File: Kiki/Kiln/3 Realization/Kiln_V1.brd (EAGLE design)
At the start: 100 x 80 mm, 19 parts, among them T1 2N3904, T2 2N3904, T3 2N3904, T4 2N3904

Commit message: Updated: 3.3v & GND Disconnected the 3.3v pin -- the was a supply pin, not a power in pin. Attached the GND for the transistors to BOTH Arduino ground pins, and beefec up the trace, just in case.  I wonder if this is enough to dump the transistors, when all segments of the digit are illuminated?
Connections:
- removed net N$30: JP3.8, PCB1.3.3V
- net GND: now also PCB1.GND., PCB1.GND..
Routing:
- net N$30: track 69.9 -> 0.00 mm
- net GND: track 35.6 -> 66.0 mm
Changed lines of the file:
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@@
 <wire x1="68.58" y1="59.69" x2="68.58" y2="50.38" width="0.4064" layer="1"/>
-</signal>
-<signal name="N$30">
-<contactref element="JP3" pad="8"/>
-<contactref element="PCB1" pad="3.3V"/>
-<wire x1="41.91" y1="49.53" x2="41.91" y2="53.34" width="0.4064" layer="1"/>
-<wire x1="41.91" y1="53.34" x2="36.83" y2="53.34" width="0.4064" layer="1"/>
-<wire x1="36.83" y1="53.34" x2="36.83" y2="15.24" width="0.4064" layer="1"/>
-<wire x1="36.83" y1="15.24" x2="55.88" y2="15.24" width="0.4064" layer="1"/>
-<wire x1="55.88" y1="15.24" x2="55.88" y2="11.43" width="0.4064" layer="1"/>
 </signal>
 <signal name="N$31">
 <contactref element="JP3" pad="9"/>
 <contactref element="PCB1" pad="VIN"/>
-<wire x1="39.37" y1="49.53" x2="39.37" y2="17.78" width="0.4064" layer="1"/>
-<wire x1="39.37" y1="17.78" x2="58.42" y2="17.78" width="0.4064" layer="1"/>
-<wire x1="58.42" y1="17.78" x2="58.42" y2="13.97" width="0.4064" layer="1"/>
-<wire x1="58.42" y1="13.97" x2="66.04" y2="13.97" width="0.4064" layer="1"/>
-<wire x1="66.04" y1="13.97" x2="66.04" y2="11.43" width="0.4064" layer="1"/>
+<wire x1="66.04" y1="11.43" x2="66.04" y2="17.78" width="0.4064" layer="16"/>
+<wire x1="66.04" y1="17.78" x2="58.42" y2="17.78" width="0.4064" layer="16"/>
+<wire x1="58.42" y1="17.78" x2="58.42" y2="24.13" width="0.4064" layer="16"/>
+<wire x1="58.42" y1="24.13" x2="39.37" y2="24.13" width="0.4064" layer="16"/>
+<wire x1="39.37" y1="24.13" x2="39.37" y2="49.53" width="0.4064" layer="16"/>
 </signal>
 <signal name="N$28">
@@
 <contactref element="T2" pad="3"/>
 <contactref element="T1" pad="3"/>
+<contactref element="PCB1" pad="GND."/>
+<contactref element="PCB1" pad="GND.."/>
+<wire x1="60.96" y1="16.51" x2="60.96" y2="11.43" width="0.4064" layer="1"/>
+<wire x1="63.5" y1="11.43" x2="63.5" y2="16.51" width="0.4064" layer="1"/>
+<wire x1="86.36" y1="26.67" x2="78.74" y2="26.67" width="0.8128" layer="1"/>
+<wire x1="78.74" y1="26.67" x2="71.12" y2="26.67" width="0.8128" layer="1"/>
+<wire x1="71.12" y1="26.67" x2="63.5" y2="26.67" width="0.8128" layer="1"/>
+<wire x1="63.5" y1="26.67" x2="58.42" y2="26.67" width="0.8128" layer="1"/>
+<wire x1="58.42" y1="26.67" x2="58.42" y2="16.51" width="0.8128" layer="1"/>
+<wire x1="58.42" y1="16.51" x2="60.96" y2="16.51" width="0.8128" layer="1"/>
+<wire x1="60.96" y1="16.51" x2="63.5" y2="16.51" width="0.8128" layer="1"/>
+<wire x1="86.36" y1="22.86" x2="86.36" y2="26.67" width="0.4064" layer="1"/>
+<wire x1="78.74" y1="24.13" x2="78.74" y2="26.67" width="0.4064" layer="1"/>
+<wire x1="71.12" y1="24.13" x2="71.12" y2="26.67" width="0.4064" layer="1"/>
 <wire x1="63.5" y1="22.86" x2="63.5" y2="26.67" width="0.4064" layer="1"/>
-<wire x1="63.5" y1="26.67" x2="71.12" y2="26.67" width="0.4064" layer="1"/>
-<wire x1="71.12" y1="24.13" x2="71.12" y2="26.67" width="0.4064" layer="1"/>
-<wire x1="71.12" y1="26.67" x2="78.74" y2="26.67" width="0.4064" layer="1"/>
-<wire x1="78.74" y1="24.13" x2="78.74" y2="26.67" width="0.4064" layer="1"/>
-<wire x1="78.74" y1="26.67" x2="86.36" y2="26.67" width="0.4064" layer="1"/>
-<wire x1="86.36" y1="26.67" x2="86.36" y2="22.86" width="0.4064" layer="1"/>
 </signal>
 <signal name="N$9">

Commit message: Update: minor changes Changed the name of the Thermal Amplifier JP3 connector, for clarity.
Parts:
- renumbered JP3 to JP3-THERM-AMP
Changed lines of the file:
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@@
 <element name="T3" library="transistor" package="TO92" value="2N3904" x="77.47" y="24.13" rot="R180"/>
 <element name="T4" library="transistor" package="TO92" value="2N3904" x="85.09" y="22.86" rot="R180"/>
-<element name="JP3" library="microbuilder" package="1X09_ROUND_70" value="" x="49.53" y="49.53" rot="R180"/>
+<element name="JP3-THERM-AMP" library="microbuilder" package="1X09_ROUND_70" value="" x="49.53" y="49.53" rot="R180"/>
 </elements>
 <signals>
@@
 </signal>
 <signal name="DRDY">
-<contactref element="JP3" pad="1"/>
+<contactref element="JP3-THERM-AMP" pad="1"/>
 </signal>
 <signal name="SCK">
-<contactref element="JP3" pad="6"/>
+<contactref element="JP3-THERM-AMP" pad="6"/>
 <contactref element="PCB1" pad="13"/>
 <wire x1="49.276" y1="59.69" x2="49.53" y2="59.69" width="0.4064" layer="1"/>
@@
 </signal>
 <signal name="SDO">
-<contactref element="JP3" pad="5"/>
+<contactref element="JP3-THERM-AMP" pad="5"/>
 <contactref element="PCB1" pad="12"/>
 <wire x1="51.816" y1="59.69" x2="52.07" y2="59.69" width="0.4064" layer="1"/>
@@
 </signal>
 <signal name="SDI">
-<contactref element="JP3" pad="4"/>
+<contactref element="JP3-THERM-AMP" pad="4"/>
 <contactref element="PCB1" pad="11"/>
 <wire x1="54.356" y1="59.69" x2="54.61" y2="59.69" width="0.4064" layer="1"/>
@@
 </signal>
 <signal name="!CS">
-<contactref element="JP3" pad="3"/>
+<contactref element="JP3-THERM-AMP" pad="3"/>
 <contactref element="PCB1" pad="10"/>
 <wire x1="56.896" y1="59.69" x2="57.15" y2="59.69" width="0.4064" layer="1"/>
@@
 </signal>
 <signal name="!FAULT">
-<contactref element="JP3" pad="2"/>
+<contactref element="JP3-THERM-AMP" pad="2"/>
 </signal>
 <signal name="N$22">
@@
 </signal>
 <signal name="N$31">
-<contactref element="JP3" pad="9"/>
+<contactref element="JP3-THERM-AMP" pad="9"/>
 <contactref element="PCB1" pad="VIN"/>
 <wire x1="66.04" y1="11.43" x2="66.04" y2="17.78" width="0.4064" layer="16"/>
@@
 <signal name="N$28">
 <contactref element="PCB1" pad="GND"/>
-<contactref element="JP3" pad="7"/>
+<contactref element="JP3-THERM-AMP" pad="7"/>
 <wire x1="46.736" y1="59.69" x2="46.99" y2="59.69" width="0.4064" layer="1"/>
 <wire x1="46.99" y1="59.69" x2="46.99" y2="57.15" width="0.4064" layer="1"/>

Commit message: Update: new display The display file was the wrong size.  Rebuilt it. Layout got horked, so had to rebuild it from scratch. Also added the relay and Heating indicator light.
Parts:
- removed 4DIG_7SEG1: (no value), 7-seg-disp:4DIG_7SEG
- added LED1: (no value), 1-Generic:LED3MM
- added R-REPLACE_ME: 0.1OHM-1/2W-1%(1210), SparkFun-Resistors:1210
- added U$1: 4DIG_7SEG_056, 7-seg-disp:4DIG_7SEG_056
- added X1: 3.5mm term, microbuilder:TERMBLOCK_1X2-3.5MM
- R10, R11, R8, R9: value (none) -> 4.7K
- moved JP3-THERM-AMP 16.3 mm to (39.4, 36.8), turned to 270 degrees
- moved R1 5.08 mm to (63.5, 54.6)
- moved R2 5.08 mm to (66.0, 54.6)
- moved R3 5.08 mm to (68.6, 54.6)
- moved R4 5.08 mm to (71.1, 54.6)
- moved R5 5.08 mm to (73.7, 54.6)
- moved R6 5.08 mm to (76.2, 54.6)
- moved R7 5.08 mm to (78.7, 54.6)
- moved R10 4.58 mm to (76.2, 15.2)
- moved R11 4.58 mm to (78.7, 15.2)
- moved R8 4.58 mm to (71.1, 15.2)
- moved R9 4.58 mm to (73.7, 15.2)
- moved FRAME1 1.27 mm to (17.8, 81.3)
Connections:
- removed net !FAULT: JP3-THERM-AMP.2
- removed net DRDY: JP3-THERM-AMP.1
- removed net N$28: JP3-THERM-AMP.7, PCB1.GND
- new net N$21: LED1.A, R-REPLACE_ME.2
- new net RELAY_POS: PCB1.9, R-REPLACE_ME.1, X1.1
- net GND: now also JP3-THERM-AMP.7, LED1.K, PCB1.GND, X1.2
- net N$10: now also U$1.13; no longer 4DIG_7SEG1.13
- net N$11: now also U$1.9; no longer 4DIG_7SEG1.9
- net N$12: now also U$1.4; no longer 4DIG_7SEG1.4
- net N$13: now also U$1.2; no longer 4DIG_7SEG1.2
- net N$14: now also U$1.1; no longer 4DIG_7SEG1.1
- net N$15: now also U$1.12; no longer 4DIG_7SEG1.12
- net N$16: now also U$1.5; no longer 4DIG_7SEG1.5
- net N$17: now also PCB1.A3; no longer PCB1.A5
- net N$18: now also PCB1.A2; no longer PCB1.A4
- net N$19: now also PCB1.A1; no longer PCB1.A3
- net N$20: now also PCB1.A0; no longer PCB1.A2
- net N$5: now also U$1.6; no longer 4DIG_7SEG1.6
- net N$6: now also U$1.10; no longer 4DIG_7SEG1.10
- net N$7: now also U$1.11; no longer 4DIG_7SEG1.11
- net N$8: now also U$1.14; no longer 4DIG_7SEG1.14
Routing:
- net GND: track 66.0 -> 156.9 mm, vias 0 -> 1
- net RELAY_POS: track 0.00 -> 53.1 mm, vias 0 -> 2
- net SDO: track 13.0 -> 35.8 mm, vias 0 -> 1
- net SCK: track 13.0 -> 35.8 mm
- net !CS: track 13.0 -> 35.8 mm, vias 0 -> 1
- net N$31: track 64.8 -> 41.9 mm
- net SDI: track 13.0 -> 35.3 mm, vias 0 -> 1
- net N$12: track 60.1 -> 39.8 mm, vias 1 -> 2
- net N$15: track 34.7 -> 16.9 mm, vias 0 -> 1
- net N$6: track 22.9 -> 38.1 mm, vias 0 -> 1
- net N$8: track 57.1 -> 41.9 mm, vias 0 -> 1
- net N$28: track 13.0 -> 0.00 mm
- net N$5: track 8.89 -> 21.6 mm
- net N$10: track 19.5 -> 11.9 mm
- net N$11: track 11.9 -> 19.5 mm
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
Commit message: Update: changed R12, LED Replaced these with real parts.  Cleared the ERC. But this does not follow proper guidelines.
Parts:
- removed R-REPLACE_ME: 0.1OHM-1/2W-1%(1210), SparkFun-Resistors:1210
- added R12: 330, SparkFun-Resistors:0603-RES
- JP3-THERM-AMP: value (none) -> 5V
- LED1: value (none) -> Red
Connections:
- net N$21: now also R12.2; no longer R-REPLACE_ME.2
- net RELAY_POS: now also R12.1; no longer R-REPLACE_ME.1
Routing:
- net N$21: track 7.29 -> 4.23 mm
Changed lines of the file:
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@@
 <element name="T3" library="transistor" package="TO92" value="2N3904" x="77.47" y="24.13" rot="R180"/>
 <element name="T4" library="transistor" package="TO92" value="2N3904" x="85.09" y="22.86" rot="R180"/>
-<element name="JP3-THERM-AMP" library="microbuilder" package="1X09_ROUND_70" value="" x="39.37" y="36.83" rot="R270"/>
+<element name="JP3-THERM-AMP" library="microbuilder" package="1X09_ROUND_70" value="5V" x="39.37" y="36.83" rot="R270"/>
 <element name="R8" library="SparkFun-Resistors" package="0603-RES" value="4.7K" x="71.12" y="15.24" rot="R90">
 <attribute name="PROD_ID" value="RES-07857" x="71.12" y="15.24" size="1.778" layer="27" rot="R90" display="off"/>
@@
 </element>
 <element name="U$1" library="7-seg-disp" package="4DIG_7SEG_056" value="4DIG_7SEG_056" x="66.04" y="40.64"/>
-<element name="LED1" library="1-Generic" package="LED3MM" value="" x="30.48" y="59.69"/>
-<element name="R-REPLACE_ME" library="SparkFun-Resistors" package="1210" value="0.1OHM-1/2W-1%(1210)" x="31.75" y="53.34" rot="R90">
-<attribute name="PROD_ID" value="RES-12374" x="31.75" y="53.34" size="1.778" layer="27" rot="R90" display="off"/>
-</element>
+<element name="LED1" library="1-Generic" package="LED3MM" value="Red" x="30.48" y="59.69"/>
 <element name="X1" library="microbuilder" package="TERMBLOCK_1X2-3.5MM" value="3.5mm term" x="24.13" y="58.42" rot="R270"/>
+<element name="R12" library="SparkFun-Resistors" package="0603-RES" value="330" x="29.21" y="54.61" rot="R90">
+<attribute name="PROD_ID" value="RES-00818" x="29.21" y="54.61" size="1.778" layer="27" rot="R90" display="off"/>
+</element>
 </elements>
 <signals>
@@
 <wire x1="24.13" y1="60.12" x2="26.67" y2="60.12" width="0.4064" layer="16"/>
 <wire x1="26.67" y1="60.12" x2="26.67" y2="57.15" width="0.4064" layer="16"/>
-<wire x1="26.67" y1="57.15" x2="31.75" y2="57.15" width="0.4064" layer="16"/>
-<wire x1="31.75" y1="57.15" x2="31.75" y2="59.69" width="0.4064" layer="16"/>
 <via x="63.5" y="17.78" extent="1-16" drill="0.6"/>
 <wire x1="63.5" y1="17.78" x2="63.5" y2="11.43" width="0.8128" layer="1"/>
@@
 <wire x1="63.5" y1="22.86" x2="63.5" y2="17.78" width="0.8128" layer="16"/>
 <wire x1="63.5" y1="17.78" x2="71.12" y2="17.78" width="0.8128" layer="16"/>
+<wire x1="26.67" y1="57.15" x2="31.75" y2="57.15" width="0.4064" layer="16"/>
+<wire x1="31.75" y1="57.15" x2="31.75" y2="59.69" width="0.4064" layer="16"/>
 </signal>
 <signal name="N$9">
@@
 <signal name="RELAY_POS">
 <contactref element="PCB1" pad="9"/>
-<contactref element="R-REPLACE_ME" pad="1"/>
 <wire x1="59.436" y1="59.69" x2="59.69" y2="59.69" width="0.4064" layer="1"/>
 <wire x1="59.69" y1="59.69" x2="59.69" y2="49.53" width="0.4064" layer="1"/>
 <wire x1="59.69" y1="49.53" x2="46.99" y2="49.53" width="0.4064" layer="1"/>
 <via x="46.99" y="49.53" extent="1-16" drill="0.6"/>
-<via x="31.75" y="49.53" extent="1-16" drill="0.6"/>
-<wire x1="31.75" y1="49.53" x2="31.75" y2="51.74" width="0.4064" layer="1"/>
-<wire x1="46.99" y1="49.53" x2="31.75" y2="49.53" width="0.4064" layer="16"/>
+<via x="35.56" y="49.53" extent="1-16" drill="0.6"/>
+<wire x1="46.99" y1="49.53" x2="35.56" y2="49.53" width="0.4064" layer="16"/>
 <contactref element="X1" pad="1"/>
-<wire x1="31.75" y1="51.74" x2="24.13" y2="51.74" width="0.4064" layer="1"/>
-<wire x1="24.13" y1="51.74" x2="24.13" y2="56.62" width="0.4064" layer="1"/>
-</signal>
-<signal name="N$21">
-<contactref element="R-REPLACE_ME" pad="2"/>
-<contactref element="LED1" pad="A"/>
-<wire x1="31.75" y1="55.88" x2="31.75" y2="54.94" width="0.4064" layer="1"/>
-<wire x1="31.75" y1="55.88" x2="29.21" y2="55.88" width="0.4064" layer="1"/>
-<wire x1="29.21" y1="55.88" x2="29.21" y2="59.69" width="0.4064" layer="1"/>
+<contactref element="R12" pad="1"/>
+<wire x1="24.13" y1="56.62" x2="24.13" y2="53.34" width="0.4064" layer="1"/>
+<wire x1="24.13" y1="53.34" x2="29.21" y2="53.34" width="0.4064" layer="1"/>
+<wire x1="29.21" y1="53.34" x2="29.21" y2="53.76" width="0.4064" layer="1"/>
+<wire x1="29.21" y1="53.34" x2="35.56" y2="53.34" width="0.4064" layer="1"/>
+<wire x1="35.56" y1="53.34" x2="35.56" y2="49.53" width="0.4064" layer="1"/>
 </signal>
 <signal name="N$25">
@@
 <wire x1="73.66" y1="59.69" x2="73.66" y2="55.46" width="0.4064" layer="1"/>
 </signal>
+<signal name="N$21">
+<contactref element="R12" pad="2"/>
+<contactref element="LED1" pad="A"/>
+<wire x1="29.21" y1="59.69" x2="29.21" y2="55.46" width="0.4064" layer="1"/>
+</signal>
 </signals>

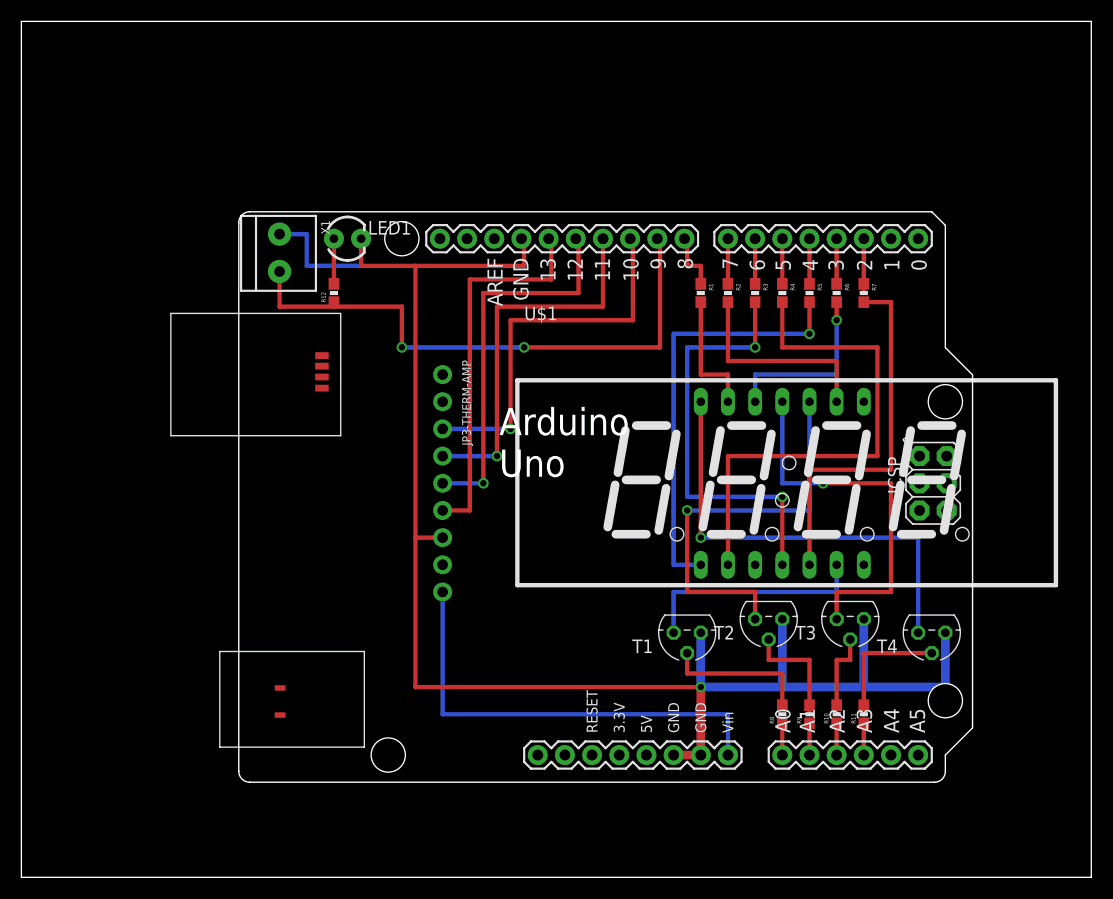
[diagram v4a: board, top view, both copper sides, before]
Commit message: Update: cleared DRC errors Have not fixed the Drill errors, but cleared the main ones.
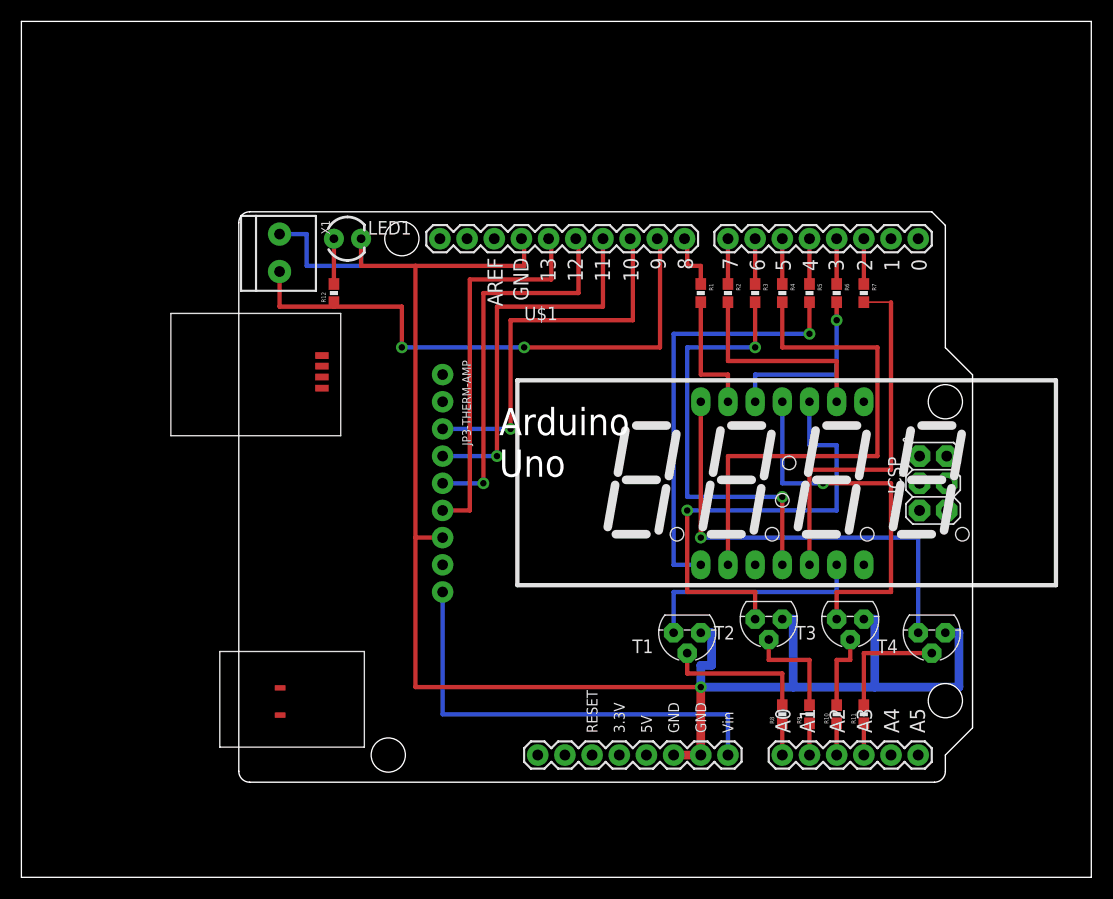
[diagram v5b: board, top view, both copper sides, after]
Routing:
- net GND: track 156.9 -> 163.5 mm
- net N$6: track 38.1 -> 43.2 mm
- net N$23: track 5.08 -> 4.23 mm
- net N$2: track 10.8 -> 9.95 mm

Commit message: Update: DRC errors cleared All the drill errors are clear now.  Some vias were eliminated. (Still need to consolidate drill sizes I think.)
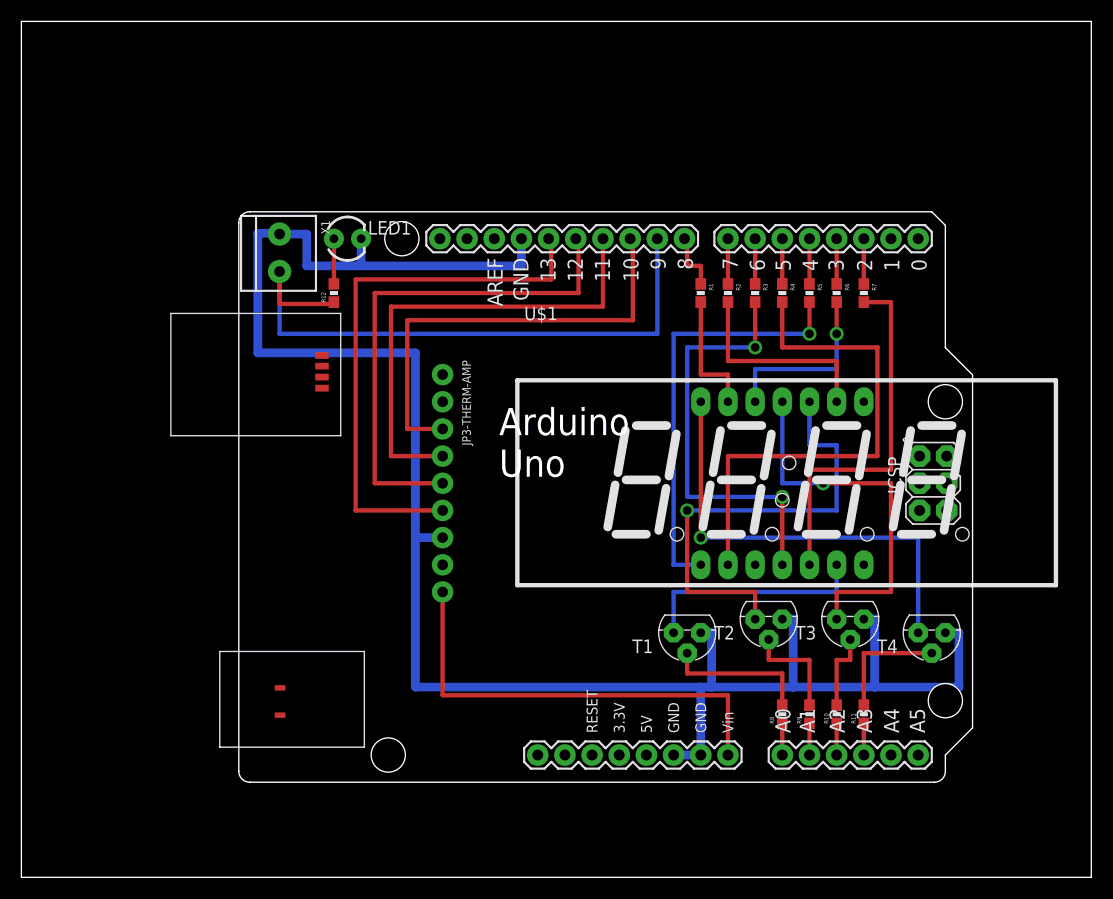
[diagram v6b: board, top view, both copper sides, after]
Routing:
- net GND: track 163.5 -> 179.8 mm, vias 1 -> 0
- net SCK: track 35.8 -> 52.1 mm
- net SDO: track 35.8 -> 48.5 mm, vias 1 -> 0
- net SDI: track 35.3 -> 45.0 mm, vias 1 -> 0
- net !CS: track 35.8 -> 42.4 mm, vias 1 -> 0
- net RELAY_POS: track 53.5 -> 58.3 mm, vias 2 -> 0
